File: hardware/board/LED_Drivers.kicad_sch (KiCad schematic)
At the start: 73 parts, among them Q901 MMBT3906

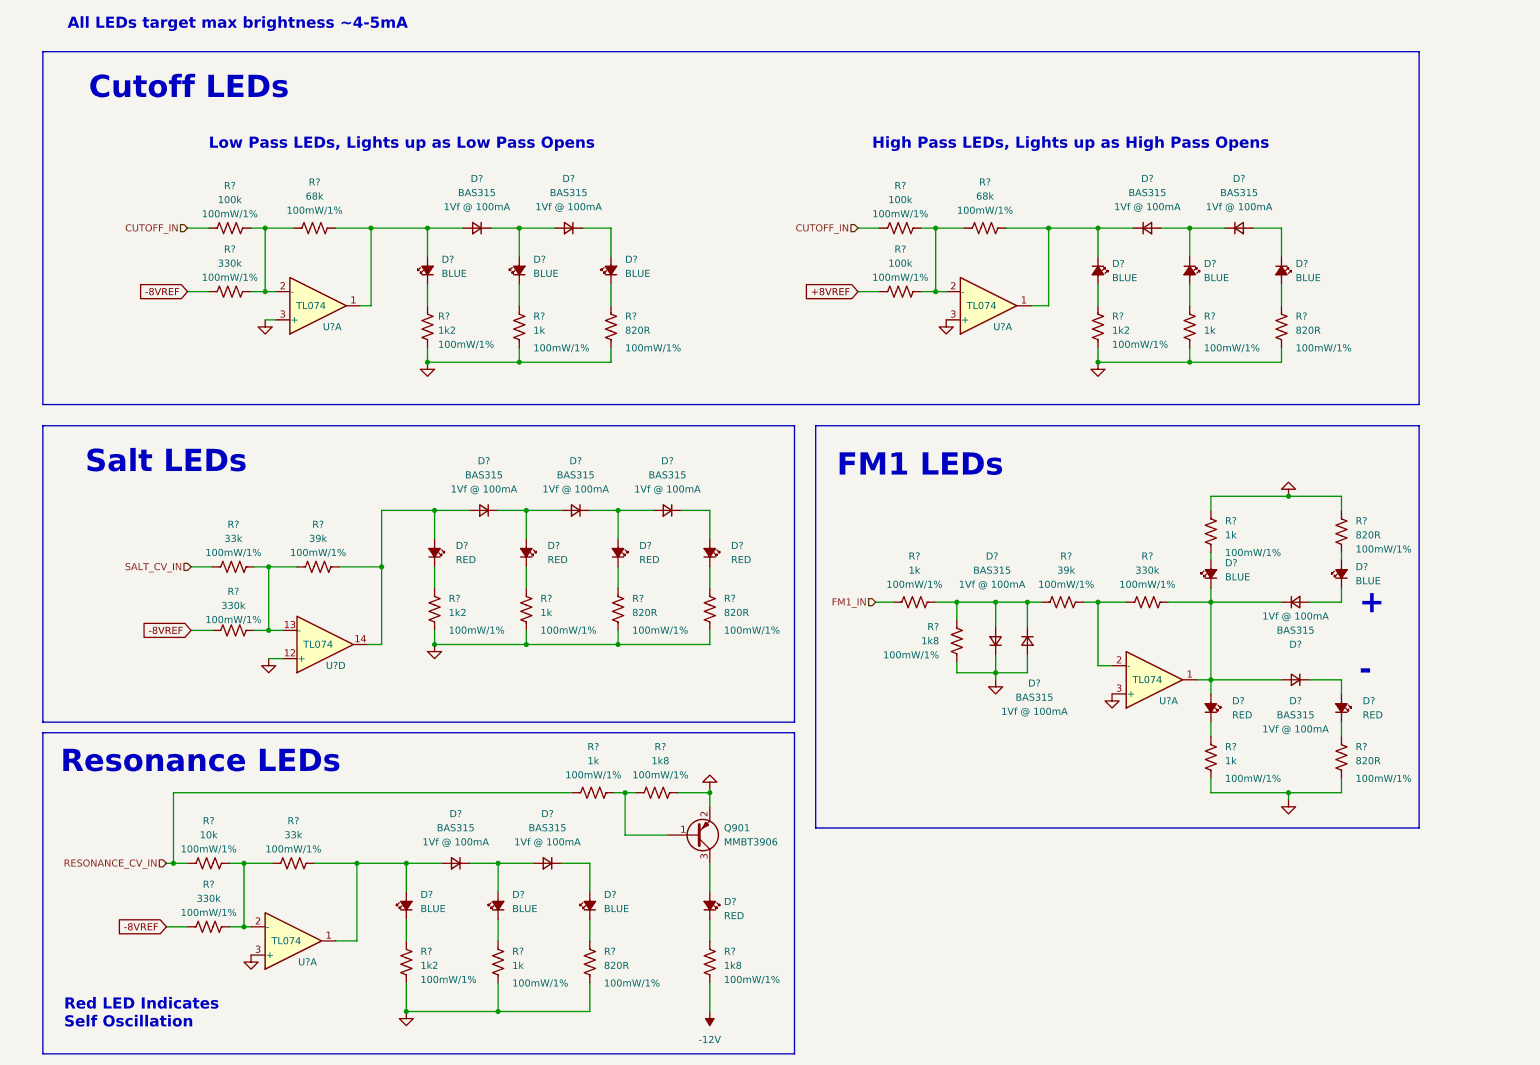
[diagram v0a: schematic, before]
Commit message: Replace 820R and 1k2 resistors with 1k resistors
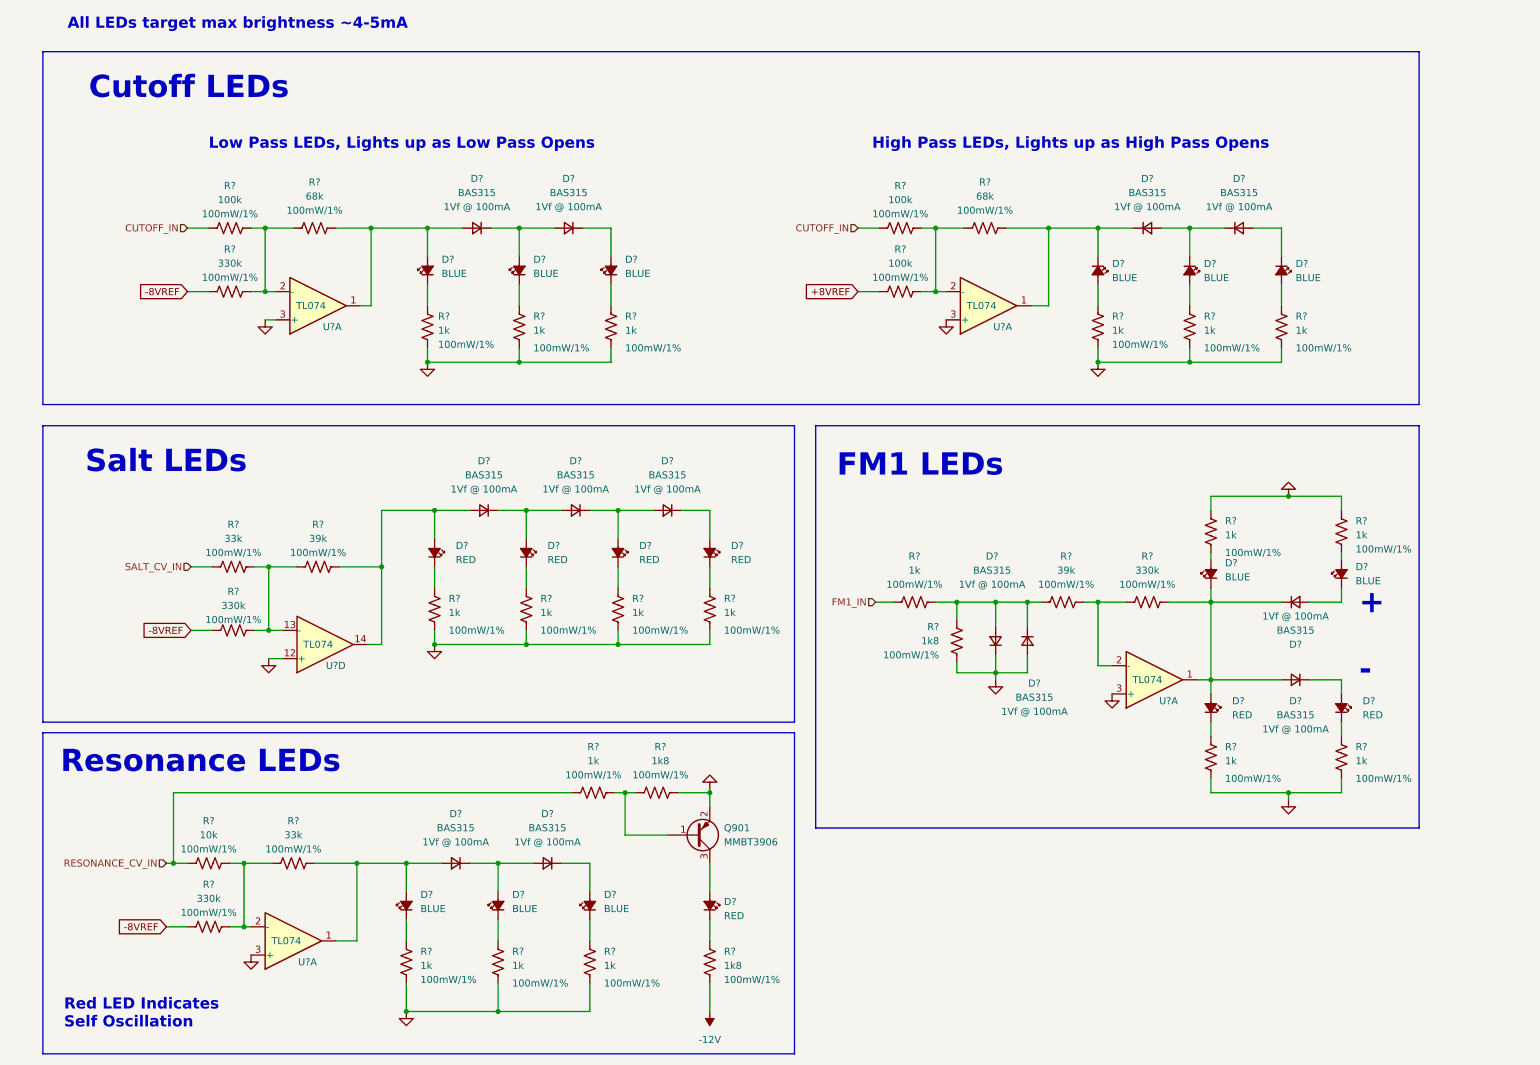
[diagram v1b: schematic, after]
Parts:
- R? (x4): value 1k2 -> 1k
- R? (x7): value 820R -> 1k
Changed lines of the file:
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@@
       (effects (font (size 1.27 1.27)) (justify left))
     )
-    (property "Value" "1k2" (at 86.995 71.755 0)
+    (property "Value" "1k" (at 86.995 71.755 0)
       (effects (font (size 1.27 1.27)) (justify left))
     )
@@
       (effects (font (size 1.27 1.27)) (justify left))
     )
-    (property "Value" "1k2" (at 88.9 122.555 0)
+    (property "Value" "1k" (at 88.9 122.555 0)
       (effects (font (size 1.27 1.27)) (justify left))
     )
@@
       (effects (font (size 1.27 1.27)) (justify left))
     )
-    (property "Value" "820R" (at 116.84 186.055 0)
+    (property "Value" "1k" (at 116.84 186.055 0)
       (effects (font (size 1.27 1.27)) (justify left))
     )
@@
       (effects (font (size 1.27 1.27)) (justify left))
     )
-    (property "Value" "1k2" (at 208.28 71.755 0)
+    (property "Value" "1k" (at 208.28 71.755 0)
       (effects (font (size 1.27 1.27)) (justify left))
     )
@@
       (effects (font (size 1.27 1.27)) (justify left))
     )
-    (property "Value" "1k2" (at 83.82 186.055 0)
+    (property "Value" "1k" (at 83.82 186.055 0)
       (effects (font (size 1.27 1.27)) (justify left))
     )
@@
       (effects (font (size 1.27 1.27)) (justify left))
     )
-    (property "Value" "820R" (at 120.65 71.755 0)
+    (property "Value" "1k" (at 120.65 71.755 0)
       (effects (font (size 1.27 1.27)) (justify left))
     )
@@
       (effects (font (size 1.27 1.27)) (justify left))
     )
-    (property "Value" "820R" (at 252.095 149.225 0)
+    (property "Value" "1k" (at 252.095 149.225 0)
       (effects (font (size 1.27 1.27)) (justify left))
     )
@@
       (effects (font (size 1.27 1.27)) (justify left))
     )
-    (property "Value" "820R" (at 241.3 71.755 0)
+    (property "Value" "1k" (at 241.3 71.755 0)
       (effects (font (size 1.27 1.27)) (justify left))
     )
@@
       (effects (font (size 1.27 1.27)) (justify left))
     )
-    (property "Value" "820R" (at 252.095 108.585 0)
+    (property "Value" "1k" (at 252.095 108.585 0)
       (effects (font (size 1.27 1.27)) (justify left))
     )
@@
       (effects (font (size 1.27 1.27)) (justify left))
     )
-    (property "Value" "820R" (at 121.92 122.555 0)
+    (property "Value" "1k" (at 121.92 122.555 0)
       (effects (font (size 1.27 1.27)) (justify left))
     )
@@
       (effects (font (size 1.27 1.27)) (justify left))
     )
-    (property "Value" "820R" (at 138.43 122.555 0)
+    (property "Value" "1k" (at 138.43 122.555 0)
       (effects (font (size 1.27 1.27)) (justify left))
     )

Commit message: hardware: add MPNs, DigiKey part numbers, and LCSC part numbers for all BOM items
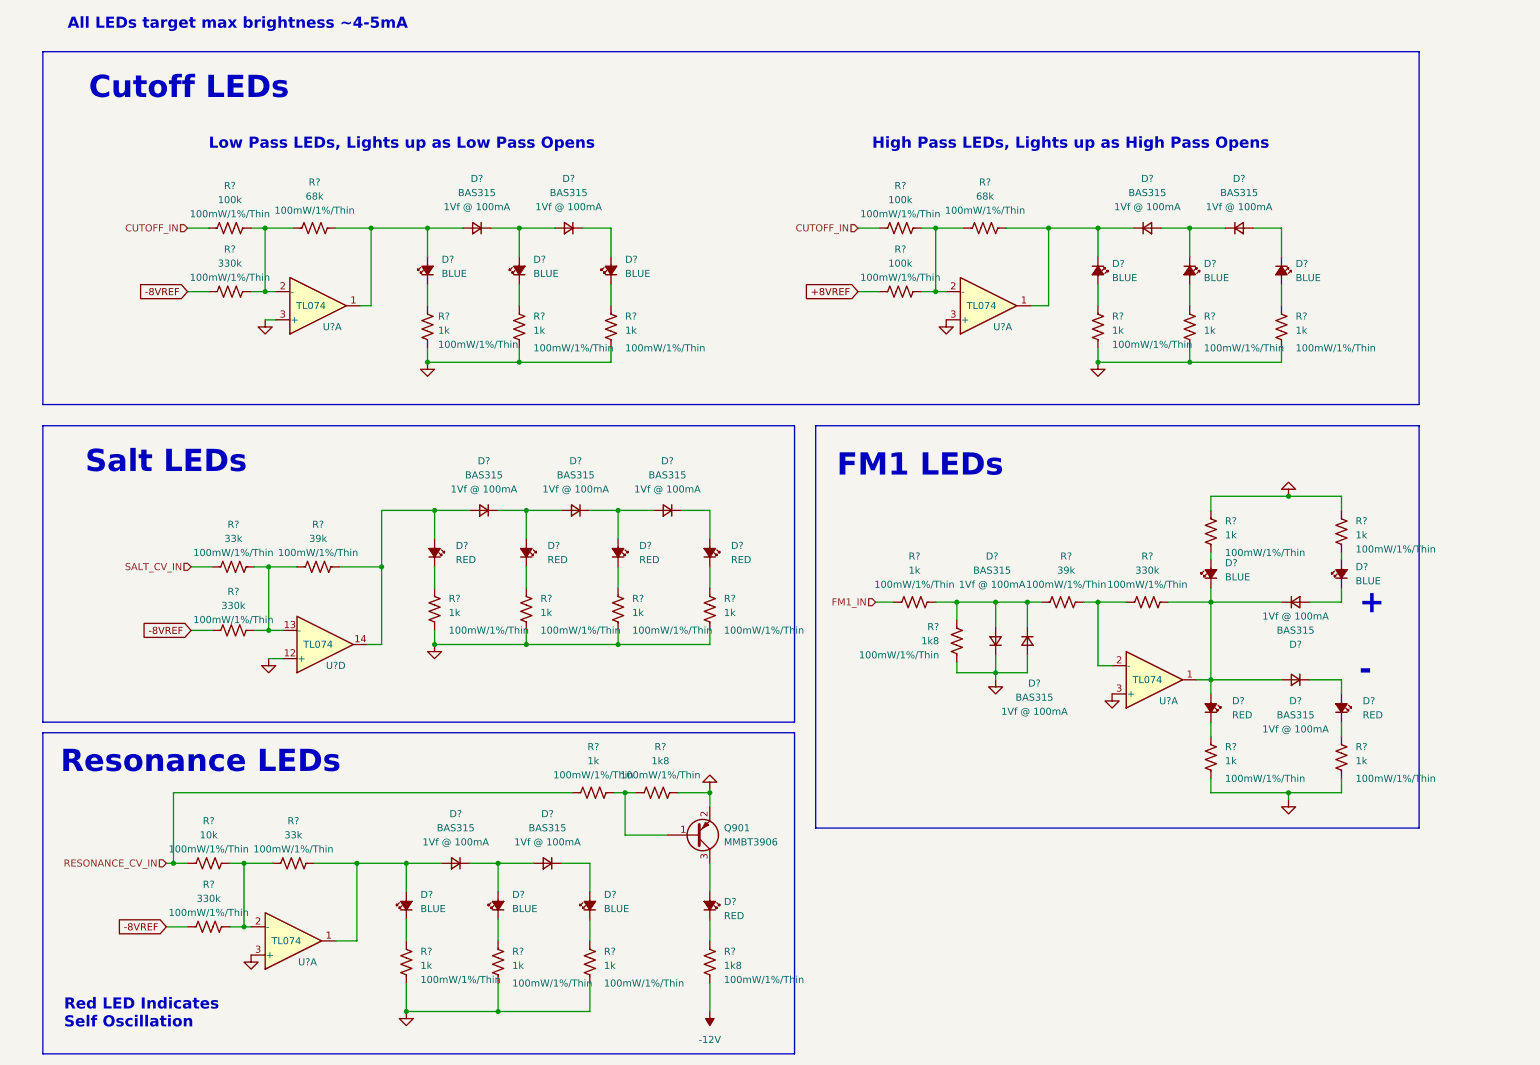
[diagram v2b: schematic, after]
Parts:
- D? (x13): DigiKey (none) -> 1727-4309-2-ND; LCSC (none) -> C109218; Substitutes Allowed (none) -> No
- D? (x7): DigiKey (none) -> 754-1133-1-ND; LCSC (none) -> C5875730; Substitutes Allowed (none) -> No
- D? (x11): DigiKey (none) -> 754-1794-1-ND; LCSC (none) -> C5879386; Substitutes Allowed (none) -> No
- Q901: DigiKey (none) -> 1727-4045-1-ND; LCSC (none) -> C75549; MPN MMBT3906 -> MMBT3906,215; Substitutes Allowed (none) -> Ask
- R? (x19): DigiKey (none) -> YAG2323TR-ND; LCSC (none) -> C375503; MPN (none) -> RT0603FRE071KL; Rating 100mW/1% -> 100mW/1%/Thin; Substitutes Allowed (none) -> Yes
- R? (x3): DigiKey (none) -> 13-RT0603FRE071K8LCT-ND; LCSC (none) -> C375505; MPN (none) -> RT0603FRE071K8L; Rating 100mW/1% -> 100mW/1%/Thin; Substitutes Allowed (none) -> Yes
- R? (x4): DigiKey (none) -> 13-RT0603FRE07330KLCT-ND; LCSC (none) -> C863745; MPN (none) -> RT0603FRE07330KL; Rating 100mW/1% -> 100mW/1%/Thin; Substitutes Allowed (none) -> Yes
- R? (x2): DigiKey (none) -> YAG5959CT-ND; LCSC (none) -> C706162; MPN (none) -> RT0603FRE0733KL; Rating 100mW/1% -> 100mW/1%/Thin; Substitutes Allowed (none) -> Yes
- R? (x3): DigiKey (none) -> 13-RT0603FRE13100KLTR-ND; LCSC (none) -> C4107493; MPN (none) -> RT0603FRE13100KL; Rating 100mW/1% -> 100mW/1%/Thin; Substitutes Allowed (none) -> Yes
- R? (x2): DigiKey (none) -> YAG5967CT-ND; LCSC (none) -> C706189; MPN (none) -> RT0603FRE0768KL; Rating 100mW/1% -> 100mW/1%/Thin; Substitutes Allowed (none) -> Yes
- R? (x2): DigiKey (none) -> 13-RT0603FRE0739KLCT-ND; LCSC (none) -> C706166; MPN (none) -> RT0603FRE0739KL; Rating 100mW/1% -> 100mW/1%/Thin; Substitutes Allowed (none) -> Yes
- R?: DigiKey (none) -> YAG2321CT-ND; LCSC (none) -> C469659; MPN (none) -> RT0603FRE0710KL; Rating 100mW/1% -> 100mW/1%/Thin; Substitutes Allowed (none) -> Yes
- U? (x5): DigiKey (none) -> 296-7198-1-ND; LCSC (none) -> C96507; MPN TL074CPW -> TL074CPWR; Substitutes Allowed (none) -> No

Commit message: hardware: update schematic fonts/text sizes, some slight readability improvements
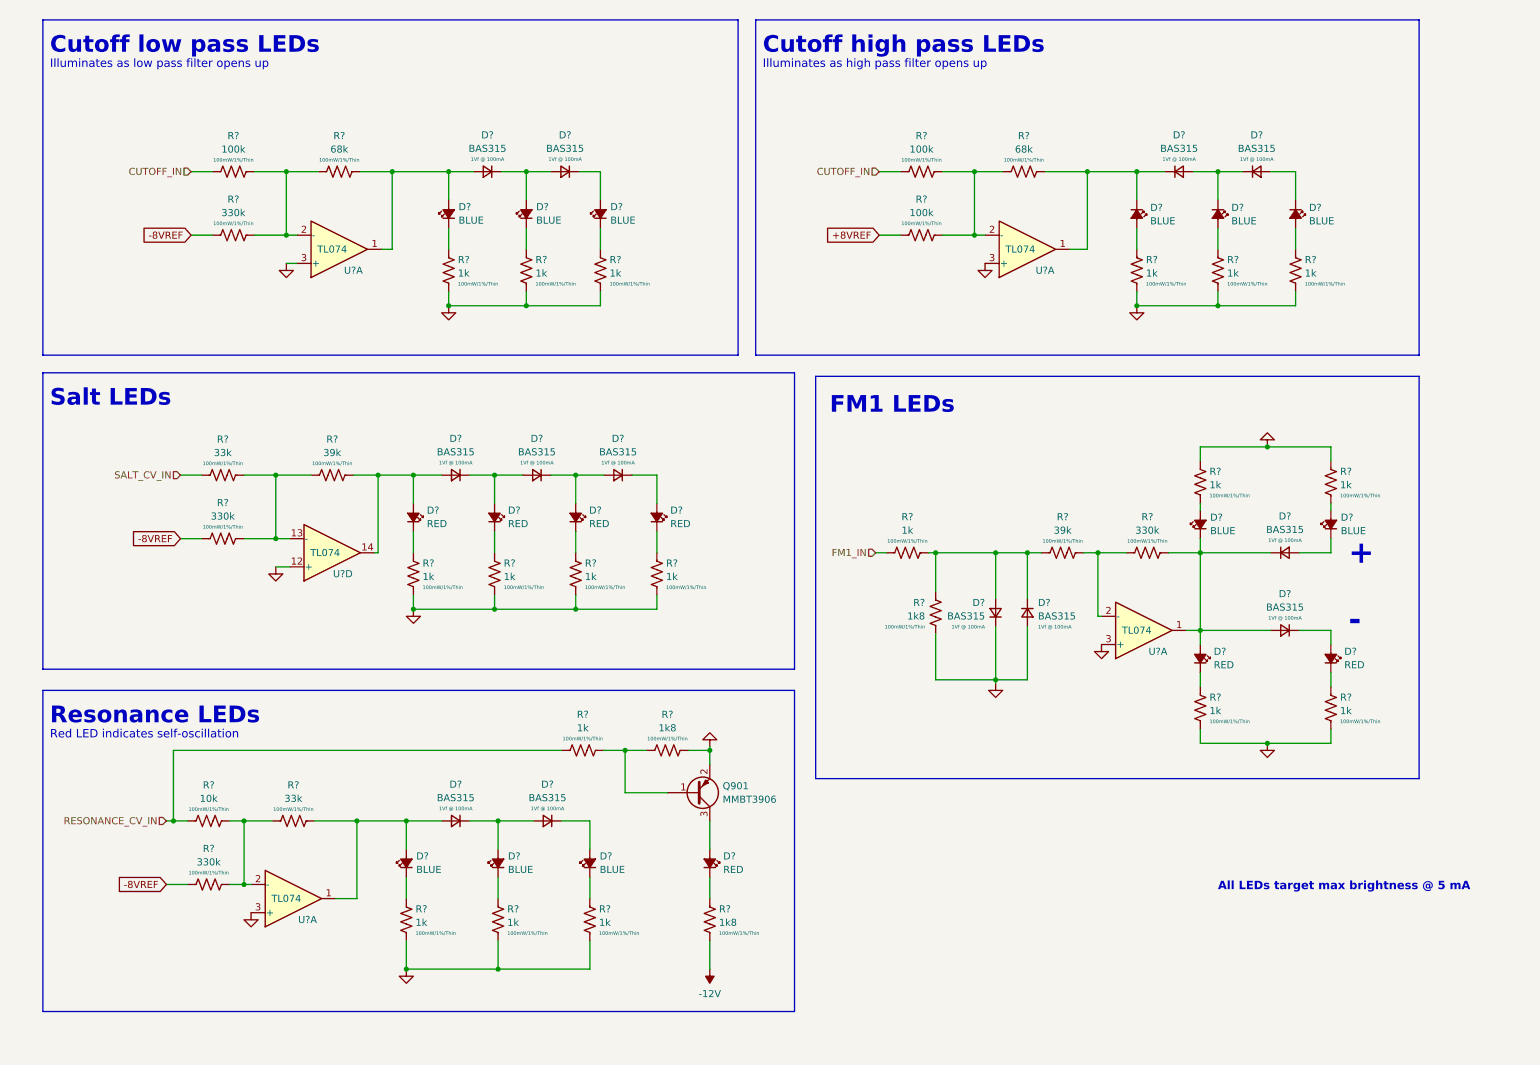
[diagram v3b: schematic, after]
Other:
- note added: "All LEDs target max brightness @ 5 mA"
- note added: "Cutoff high pass LEDs"
- note added: "Cutoff low pass LEDs"
- note added: "Illuminates as high pass filter opens up"
- note added: "Illuminates as low pass filter opens up"
- note added: "Red LED indicates self-oscillation"
- note removed: "All LEDs target max brightness ~4-5mA"
- note removed: "Cutoff LEDs"
- note removed: "High Pass LEDs, Lights up as High Pass Opens"
- note removed: "Low Pass LEDs, Lights up as Low Pass Opens"
- note removed: "Red LED Indicates Self Oscillation"
- moved on the sheet: D?, Q901, R?, U?A, U?D

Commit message: hardware: use new Winterbloom sheet layout
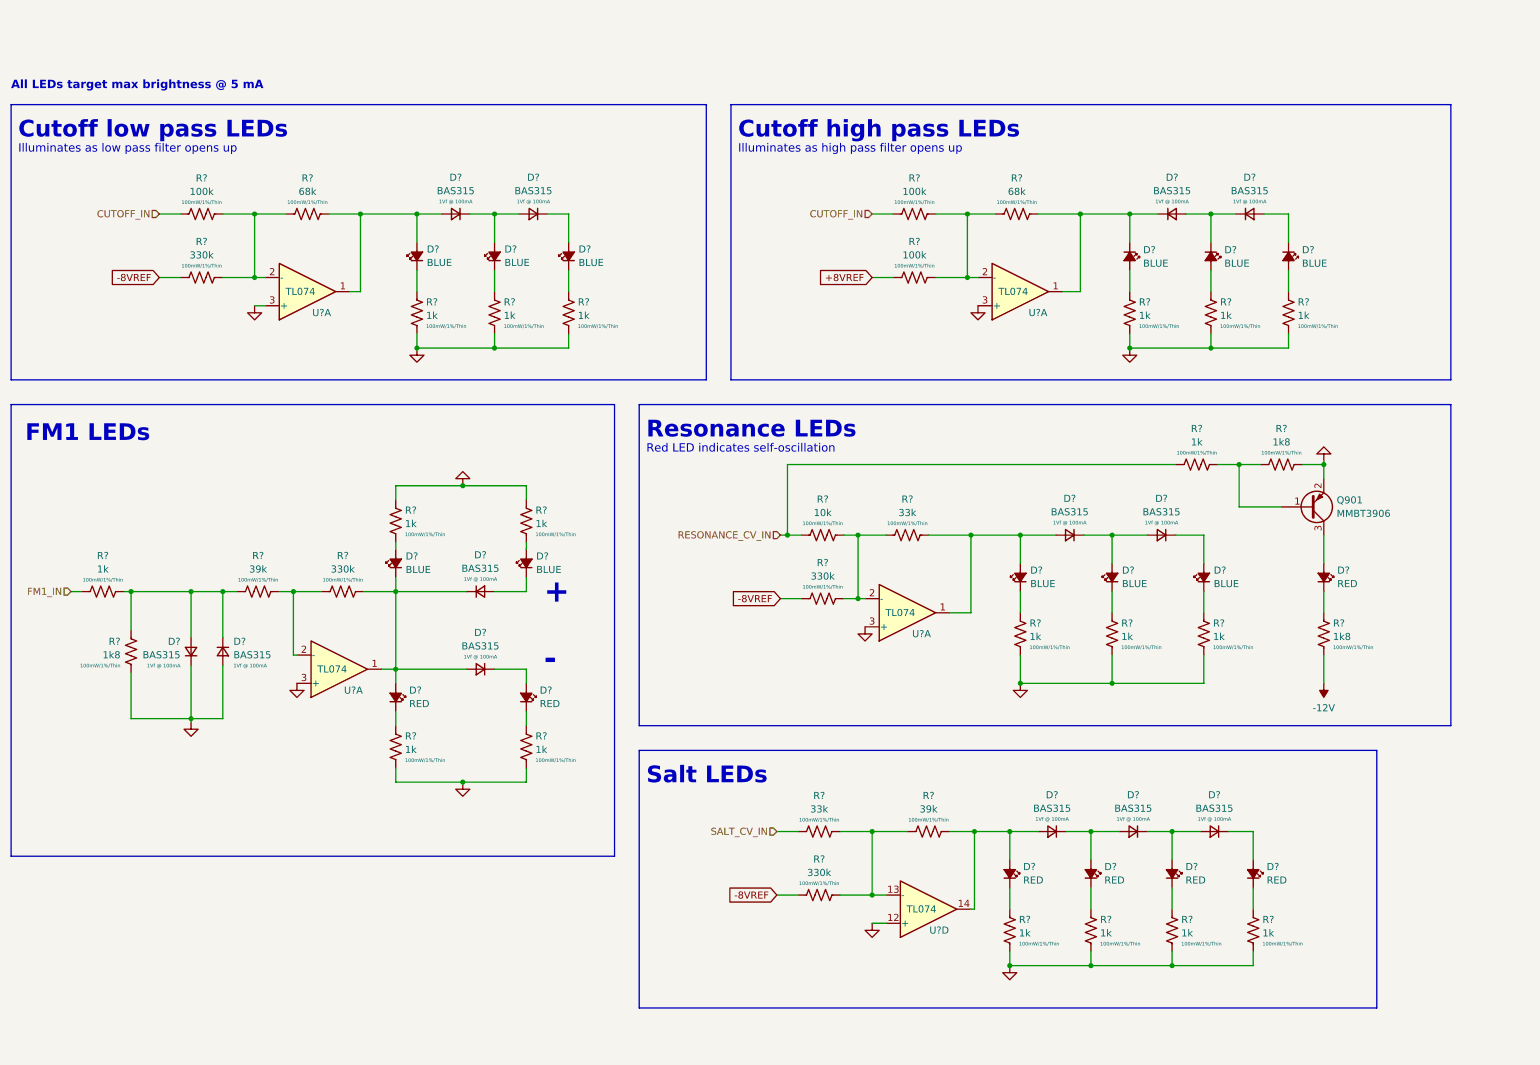
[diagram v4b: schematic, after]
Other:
- moved on the sheet: D?, Q901, R?, U?A, U?D
